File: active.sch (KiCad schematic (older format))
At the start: 33 parts, among them P1 CONN_1, P10 CONN_1, P11 CONN_1, P12 CONN_1, P2 CONN_1, P3 CONN_1, P4 CONN_1, P5 CONN_1, P6 CONN_1, P7 CONN_1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

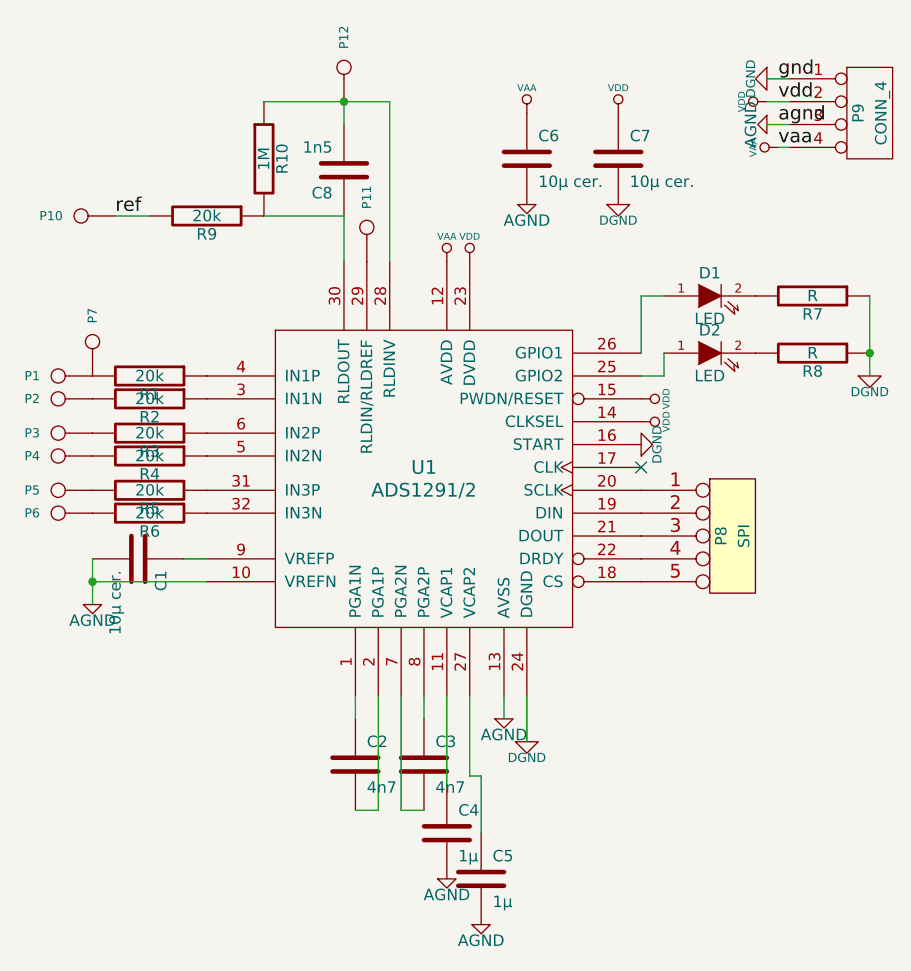
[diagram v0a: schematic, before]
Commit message: Now DRC-compliant
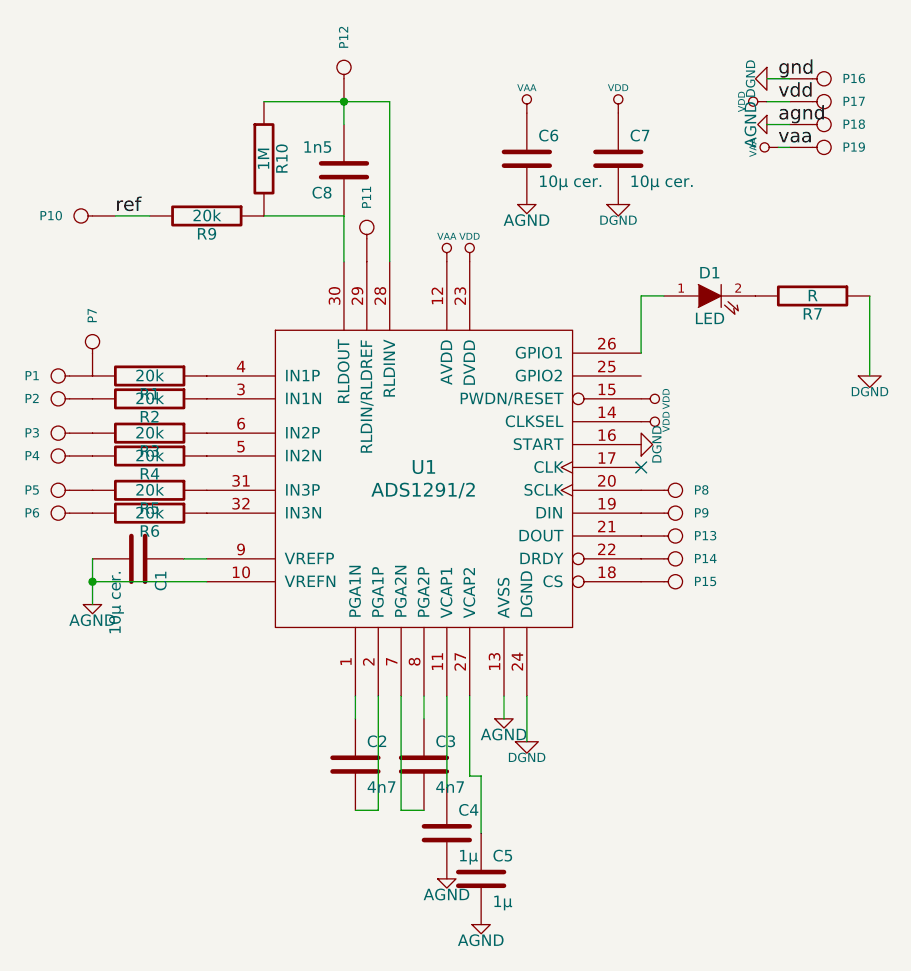
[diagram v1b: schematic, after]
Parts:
- removed D2: LED, symbol LED
- removed P8: SPI, symbol CONN_5
- removed P9: CONN_4, symbol CONN_4
- removed R8: R, symbol R
- added P13, P14, P15, P16, P17, P18, P19, P8, P9: CONN_1, symbol CONN_1
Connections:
- net AGND: now also P18.1
- net DGND: now also P16.1
- net VAA: now also P19.1
- net VDD: now also P17.1
- net at U1.18 (CS): now also P15.1
- net at U1.19 (DIN): now also P9.1
- net at U1.20 (SCLK): now also P8.1
- net at U1.21 (DOUT): now also P13.1
- net at U1.22 (DRDY): now also P14.1
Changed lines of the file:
@@
-EESchema Schematic File Version 2  date Tue 21 Feb 2012 02:41:53 PM CET
+EESchema Schematic File Version 2  date Tue 28 Feb 2012 12:25:18 PM CET
 LIBS:power
 LIBS:device
@@
 Sheet 1 1
 Title ""
-Date "16 feb 2012"
+Date "28 feb 2012"
 Rev ""
 Comp ""
@@
 Comment4 ""
 $EndDescr
+Wire Wire Line
+	6650 2000 6750 2000
+Wire Wire Line
+	6650 1800 6750 1800
+Connection ~ 4800 1900
+Wire Wire Line
+	5000 2600 5000 1900
+Wire Wire Line
+	5000 1900 4450 1900
+Wire Wire Line
+	4450 2400 4800 2400
+Wire Wire Line
+	6750 2100 6700 2100
+Wire Wire Line
+	7100 2750 7100 3100
+Connection ~ 3700 4000
+Wire Wire Line
+	3700 3900 3700 4100
+Wire Wire Line
+	5400 5100 5400 4850
+Wire Wire Line
+	5400 4850 5350 4850
+Wire Wire Line
+	5350 4850 5350 4500
+Wire Wire Line
+	5150 5000 5050 5000
+Wire Wire Line
+	5050 5000 5050 4500
+Wire Wire Line
+	4850 4600 4850 4500
+Wire Wire Line
+	5600 4500 5600 4700
+Wire Wire Line
+	5500 4500 5500 4600
+Wire Wire Line
+	5150 4600 5150 4500
+Wire Wire Line
+	4850 5000 4950 5000
+Wire Wire Line
+	4950 5000 4950 4500
+Wire Wire Line
+	5250 4900 5250 4500
+Wire Wire Line
+	3700 4000 4200 4000
+Wire Wire Line
+	4100 3900 4200 3900
+Wire Wire Line
+	6200 2750 6100 2750
+Wire Wire Line
+	6100 2750 6100 3000
+Wire Wire Line
+	4800 2400 4800 2600
+Wire Wire Line
+	4800 1900 4800 2000
+Wire Wire Line
+	3950 2400 3800 2400
+Wire Wire Line
+	6650 1900 6750 1900
+$Comp
+L CONN_1 P19
+U 1 1 4F45011B
+P 6900 2100
+F 0 "P19" H 6980 2100 40  0000 L CNN
+F 1 "CONN_1" H 6900 2155 30  0001 C CNN
+	1    6900 2100
+	1    0    0    -1
+$EndComp
+$Comp
+L CONN_1 P18
+U 1 1 4F450115
+P 6900 2000
+F 0 "P18" H 6980 2000 40  0000 L CNN
+F 1 "CONN_1" H 6900 2055 30  0001 C CNN
+	1    6900 2000
+	1    0    0    -1
+$EndComp
+$Comp
+L CONN_1 P17
+U 1 1 4F450113
+P 6900 1900
+F 0 "P17" H 6980 1900 40  0000 L CNN
+F 1 "CONN_1" H 6900 1955 30  0001 C CNN
+	1    6900 1900
+	1    0    0    -1
+$EndComp
+$Comp
+L CONN_1 P16
+U 1 1 4F45010E
+P 6900 1800
+F 0 "P16" H 6980 1800 40  0000 L CNN
+F 1 "CONN_1" H 6900 1855 30  0001 C CNN
+	1    6900 1800
+	1    0    0    -1
+$EndComp
+$Comp
+L CONN_1 P15
+U 1 1 4F450102
+P 6250 4000
+F 0 "P15" H 6330 4000 40  0000 L CNN
+F 1 "CONN_1" H 6250 4055 30  0001 C CNN
+	1    6250 4000
+	1    0    0    1
+$EndComp
+$Comp
+L CONN_1 P14
+U 1 1 4F450101
+P 6250 3900
+F 0 "P14" H 6330 3900 40  0000 L CNN
+F 1 "CONN_1" H 6250 3955 30  0001 C CNN
+	1    6250 3900
+	1    0    0    1
+$EndComp
+$Comp
+L CONN_1 P13
+U 1 1 4F4500FF
+P 6250 3800
+F 0 "P13" H 6330 3800 40  0000 L CNN
+F 1 "CONN_1" H 6250 3855 30  0001 C CNN
+	1    6250 3800
+	1    0    0    1
+$EndComp
+$Comp
+L CONN_1 P9
+U 1 1 4F4500FE
+P 6250 3700
+F 0 "P9" H 6330 3700 40  0000 L CNN
+F 1 "CONN_1" H 6250 3755 30  0001 C CNN
+	1    6250 3700
+	1    0    0    1
+$EndComp
+$Comp
+L CONN_1 P8
+U 1 1 4F4500F7
+P 6250 3600
+F 0 "P8" H 6330 3600 40  0000 L CNN
+F 1 "CONN_1" H 6250 3655 30  0001 C CNN
+	1    6250 3600
+	1    0    0    1
+$EndComp
 $Comp
 L CONN_1 P12
@@
 Text Label 6700 1800 0    60   ~ 0
 gnd
-Wire Wire Line
-	6650 2000 6750 2000
-Wire Wire Line
-	6650 1800 6750 1800
-Connection ~ 4800 1900
-Wire Wire Line
-	5000 2600 5000 1900
-Wire Wire Line
-	5000 1900 4800 1900
-Wire Wire Line
-	4800 1900 4450 1900
-Wire Wire Line
-	4450 2400 4800 2400
-Wire Wire Line
-	6750 2100 6700 2100
-Wire Wire Line
-	6200 3000 6200 3100
-Wire Wire Line
-	6200 3100 6100 3100
-Connection ~ 7100 3000
-Wire Wire Line
-	7100 2750 7100 3000
-Wire Wire Line
-	7100 3000 7100 3100
-Connection ~ 3700 4000
-Wire Wire Line
-	3700 3900 3700 4000
-Wire Wire Line
-	3700 4000 3700 4100
-Wire Wire Line
-	5400 5100 5400 4850
-Wire Wire Line
-	5400 4850 5350 4850
-Wire Wire Line
-	5350 4850 5350 4500
-Wire Wire Line
-	5150 5000 5050 5000
-Wire Wire Line
-	5050 5000 5050 4500
-Wire Wire Line
-	4850 4600 4850 4500
-Wire Wire Line
-	5600 4500 5600 4700
-Wire Wire Line
-	5500 4500 5500 4600
-Wire Wire Line
-	5150 4600 5150 4500
-Wire Wire Line
-	4850 5000 4950 5000
-Wire Wire Line
-	4950 5000 4950 4500
-Wire Wire Line
-	5250 4900 5250 4500
-Wire Wire Line
-	3700 4000 4200 4000
-Wire Wire Line
-	4100 3900 4200 3900
-Wire Wire Line
-	6200 2750 6100 2750
-Wire Wire Line
-	6100 2750 6100 3000
-Wire Wire Line
-	4800 2400 4800 2600
-Wire Wire Line
-	4800 1900 4800 2000
-Wire Wire Line
-	3950 2400 3800 2400
-Wire Wire Line
-	6650 1900 6750 1900
 Text Label 3800 2400 0    60   ~ 0
 ref
@@
 $EndComp
 $Comp
-L CONN_4 P9
-U 1 1 4EFCC876
-P 7100 1950
-F 0 "P9" V 7050 1950 50  0000 C CNN
-F 1 "CONN_4" V 7150 1950 50  0000 C CNN
-	1    7100 1950
-	1    0    0    -1
-$EndComp
-$Comp
 L VDD #PWR16
 U 1 1 4EFCC86C
@@
 NoConn ~ 6100 3500
 $Comp
-L CONN_5 P8
-U 1 1 4EFCC439
-P 6500 3800
-F 0 "P8" V 6450 3800 50  0000 C CNN
-F 1 "SPI" V 6550 3800 50  0000 C CNN
-	1    6500 3800
-	1    0    0    -1
-$EndComp
-$Comp
 L VDD #PWR13
 U 1 1 4EFCC375
@@
 $EndComp
 $Comp
-L R R8
-U 1 1 4EFCC270
-P 6850 3000
-F 0 "R8" V 6930 3000 50  0000 C CNN
-F 1 "R" V 6850 3000 50  0000 C CNN
-	1    6850 3000
-	0    1    1    0
-$EndComp
-$Comp
 L R R7
 U 1 1 4EFCC26C
@@
 $EndComp
 $Comp
-L LED D2
-U 1 1 4EFCC261
-P 6400 3000
-F 0 "D2" H 6400 3100 50  0000 C CNN
-F 1 "LED" H 6400 2900 50  0000 C CNN
-	1    6400 3000
-	1    0    0    -1
-$EndComp
-$Comp

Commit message: Made the pads at the pcb corners larger. Made the pad clearance of the battery connector on the bottom layer larger.
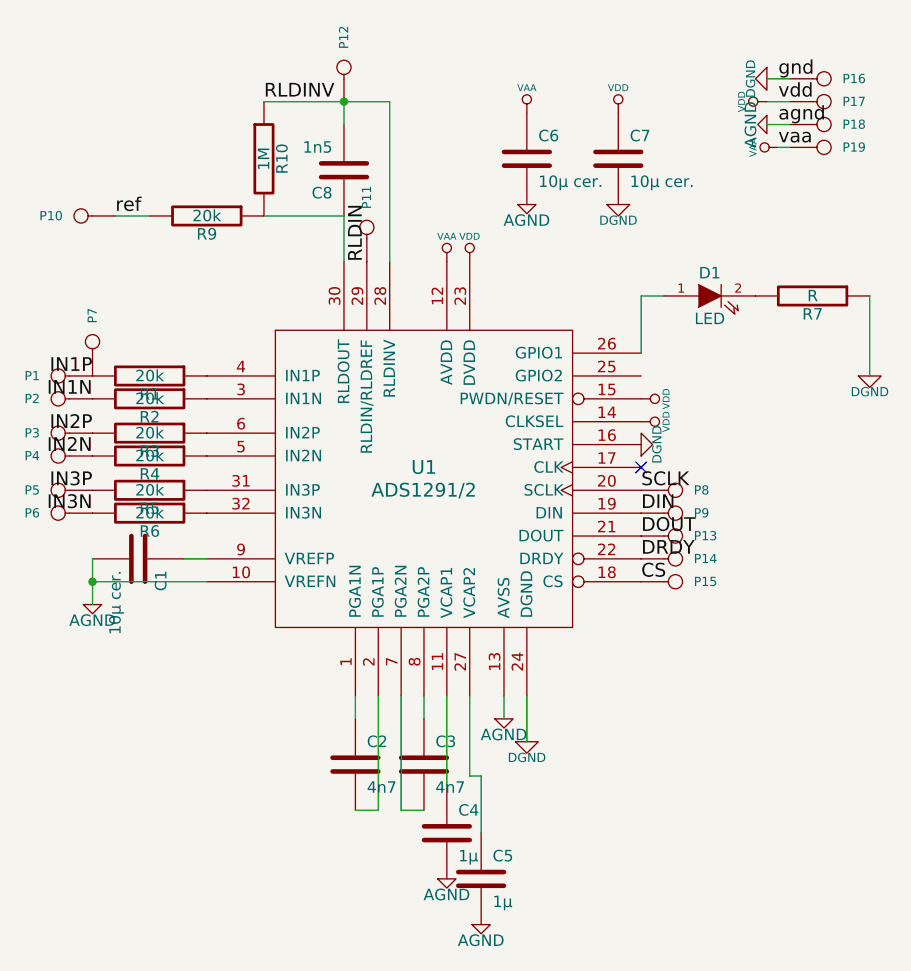
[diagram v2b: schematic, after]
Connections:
- net CS: now reaches P15.1, U1.18 (CS)
- net DIN: now reaches P9.1, U1.19 (DIN)
- net SCLK: now reaches P8.1, U1.20 (SCLK)
- net DOUT: now reaches P13.1, U1.21 (DOUT)
- net DRDY: now reaches P14.1, U1.22 (DRDY)
- net RLDINV: now reaches C8.2, P12.1, R10.1, U1.28 (RLDINV)
- net RLDIN: now reaches P11.1, U1.29 (RLDIN/RLDREF)
- net IN1P: now reaches P1.1, P7.1, R1.2
- net IN1N: now reaches P2.1, R2.2
- net IN2P: now reaches P3.1, R3.2
- net IN2N: now reaches P4.1, R4.2
- net IN3P: now reaches P5.1, R5.2
- net IN3N: now reaches P6.1, R6.2
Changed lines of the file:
@@
-EESchema Schematic File Version 2  date Tue 28 Feb 2012 12:25:18 PM CET
+EESchema Schematic File Version 2  date Sat 03 Mar 2012 05:15:58 PM CET
 LIBS:power
 LIBS:device
@@
 Sheet 1 1
 Title ""
-Date "28 feb 2012"
+Date "3 mar 2012"
 Rev ""
 Comp ""
@@
 Comment4 ""
 $EndDescr
+Text Label 3700 3700 2    60   ~ 0
+IN3N
+Text Label 3700 3600 2    60   ~ 0
+IN3P
+Text Label 3700 3450 2    60   ~ 0
+IN2N
+Text Label 3700 3350 2    60   ~ 0
+IN2P
+Text Label 3700 3200 2    60   ~ 0
+IN1N
+Text Label 3700 3100 2    60   ~ 0
+IN1P
+Text Label 6100 4000 0    60   ~ 0
+CS
+Text Label 6100 3900 0    60   ~ 0
+DRDY
+Text Label 6100 3800 0    60   ~ 0
+DOUT
+Text Label 6100 3700 0    60   ~ 0
+DIN
+Text Label 6100 3600 0    60   ~ 0
+SCLK
+Text Label 4450 1900 0    60   ~ 0
+RLDINV
+Text Label 4900 2600 1    60   ~ 0
+RLDIN
 Wire Wire Line
 	6650 2000 6750 2000
